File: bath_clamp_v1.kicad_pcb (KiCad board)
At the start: 6 copper layers, 127 x 76.2 mm, 154 parts, among them IC1 DAC53401DSGR, J1 105-1103-001, J2 105-1103-001, J3 105-1103-001, J4 HDMI_A, K1 1462042-8, K2 1462042-8, Q1 MBT3904DW1T1G, Q2 BC856, Q3 MBT3904DW1T1G, Q4 MBT3904DW1T1G, U1 OPA828, U10 LP2951-3.3_SOIC, U11 OPA991S, U12 TCA9555DBR, U13 TCA9555DBR, U14 DG412xUE, U15 OPA828, U16 TMUX6111PWR, U17 DG412xUE, U18 AD8421ARZ, U19 TMUX6136PWR, U2 ADG1208, U20 TMUX6111PWR, U21 TMUX6111PWR, U22 TMUX6136PWR, U23 OPA188xxDBV, U24 LMP8350MA_NOPB, U25 OPA2156xD, U3 G6L-1F-TR-DC5, U4 G6L-1F-TR-DC5, U5 G6L-1F-TR-DC5, U6 24AA025UID, U7 LM337L_SO8, U8 OPA2156xD, U9 MCP1804x-3302xOT

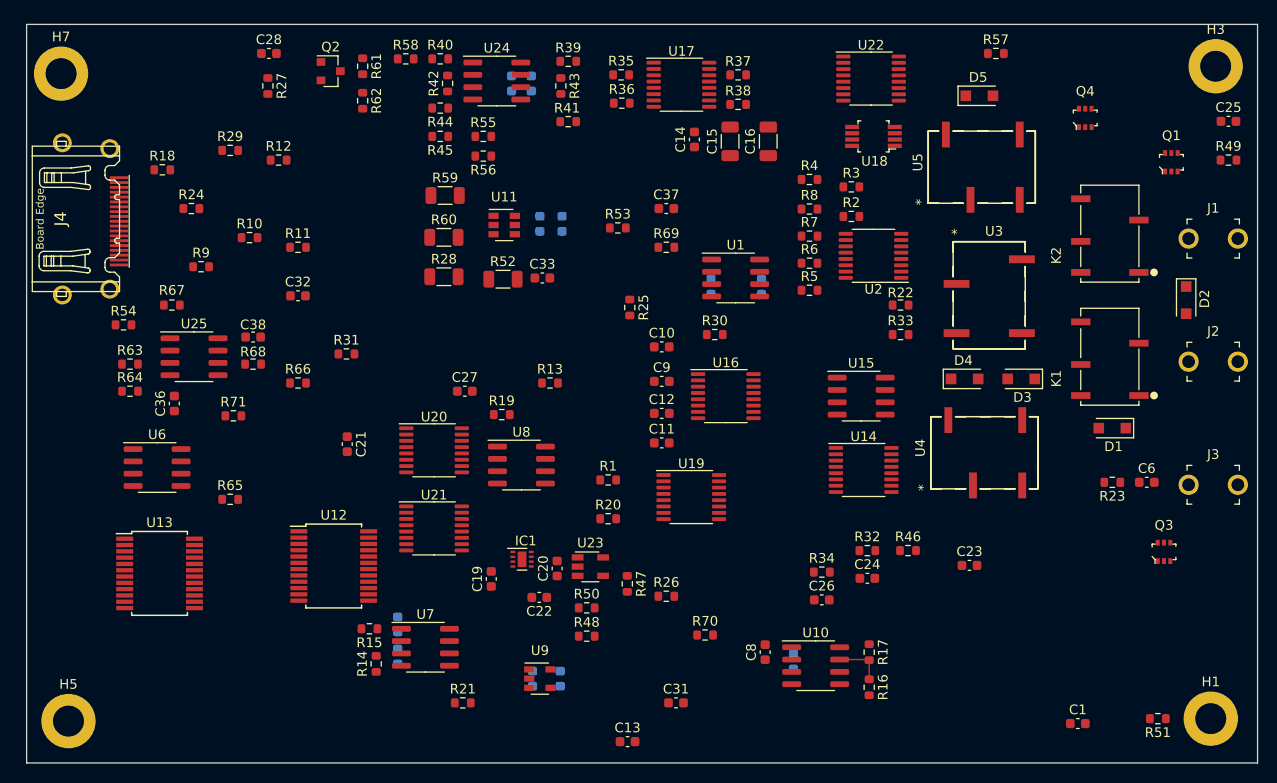
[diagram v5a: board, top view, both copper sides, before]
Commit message: first freerouter trial of routing
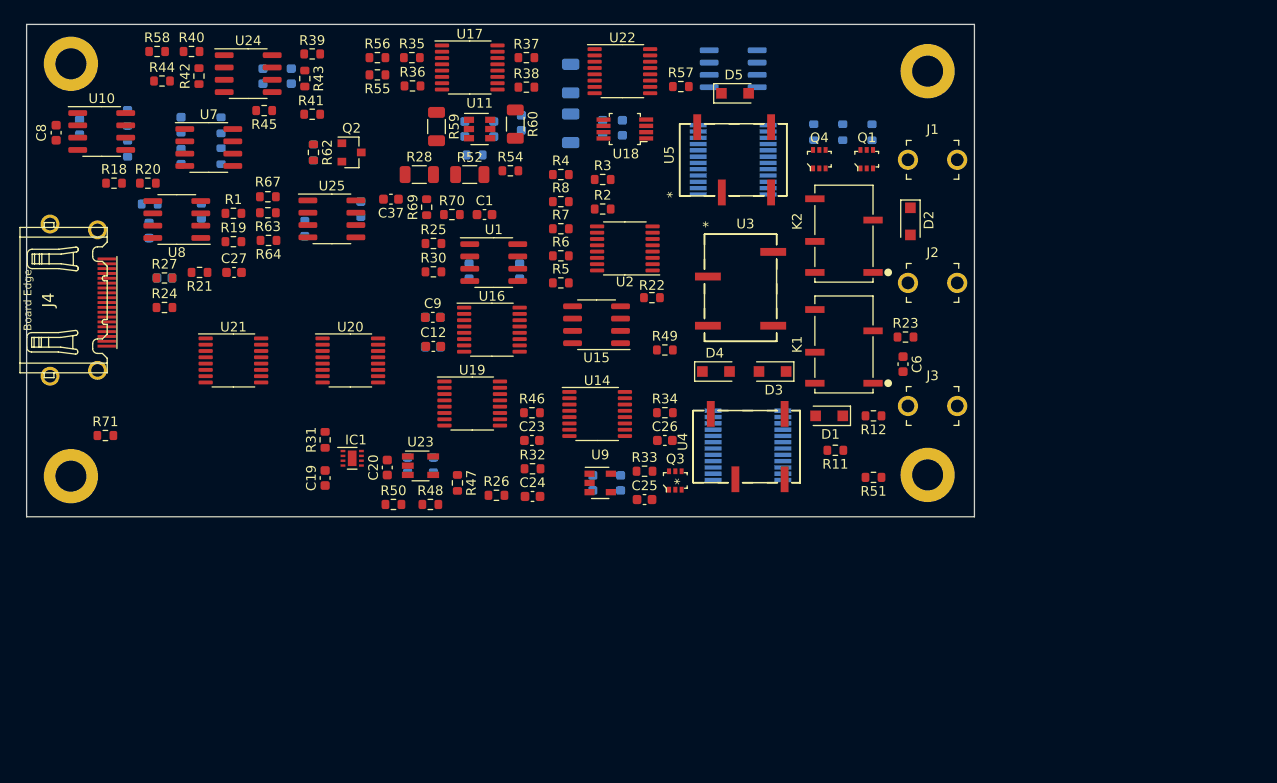
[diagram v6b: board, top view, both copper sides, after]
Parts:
- removed R65, R66, R68: 0, Resistor_SMD:R_0603_1608Metric
- C10, C11, C13, C14, C15, C16, C21, C22, C28, C31, C32, C33, C36, C38, R10, R13, R14, R15, R16, R17, R29, R53, R61, R9, U12, U13, U6: moved to B.Cu
- moved R16 94.6 mm to (10.4, 12.8)
- moved R17 94.3 mm to (10.4, 9.65)
- moved C7 92.0 mm to (5.46, 10.6)
- moved U10 92.0 mm to (7.75, 11.0)
- moved C8 90.7 mm to (3.05, 11.2), turned to 270 degrees
- moved C1 80.7 mm to (47.2, 19.6)
- moved U13 73.0 mm to (72.9, 14.0)
- moved U6 72.3 mm to (72.9, 4.57)
- moved C25 71.8 mm to (63.8, 49.0)
- moved C31 70.5 mm to (18.0, 19.2), turned to 90 degrees
- moved R12 66.8 mm to (87.4, 40.4), turned to 180 degrees
- moved R9 64.7 mm to (81.2, 11.1), turned to 270 degrees
- moved C13 63.3 mm to (61.5, 10.7), turned to 90 degrees
- moved R10 62.2 mm to (84.2, 11.1), turned to 270 degrees
- moved R49 61.4 mm to (65.8, 33.6)
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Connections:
- C1 pad 1: /bath_clamp_v1_1/RF_1 -> Net-(C1-Pad1)
- C1 pad 2: Net-(C1-Pad2) -> /bath_clamp_v1_1/RF_1
- R31 pad 1: GND -> Net-(IC1-Pad1)
- R31 pad 2: Net-(IC1-Pad1) -> GND
- R46 pad 1: Net-(C23-Pad2) -> Net-(C23-Pad1)
- R46 pad 2: Net-(C23-Pad1) -> Net-(C23-Pad2)
- R69 pad 1: Net-(C37-Pad1) -> /bath_clamp_v1_1/compensation_switching/OUT
- R69 pad 2: /bath_clamp_v1_1/compensation_switching/OUT -> Net-(C37-Pad1)
- R70 pad 1: Net-(C1-Pad2) -> /bath_clamp_v1_1/compensation_switching/OUT
- R70 pad 2: /bath_clamp_v1_1/compensation_switching/OUT -> Net-(C1-Pad1)
- U25 pad 5: Net-(R65-Pad1) -> GND
- U25 pad 6: Net-(R66-Pad1) -> GND
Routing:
- net Net-(R16-Pad1): track 5.05 -> 0.00 mm
- net (no net): track 0.00 -> 0.74 mm
- added copper zone on Route14, net +15V
- added copper zone on Route3, net +5V
- added copper zone on Route15, net -15V
- added copper zone on Route2, net GND
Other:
- board size 127 x 76.2 mm -> 97.8 x 50.8 mm
- net class Power added: clearance 0.2032, trace_width 0.508, via_dia 0.889, via_drill 0.381

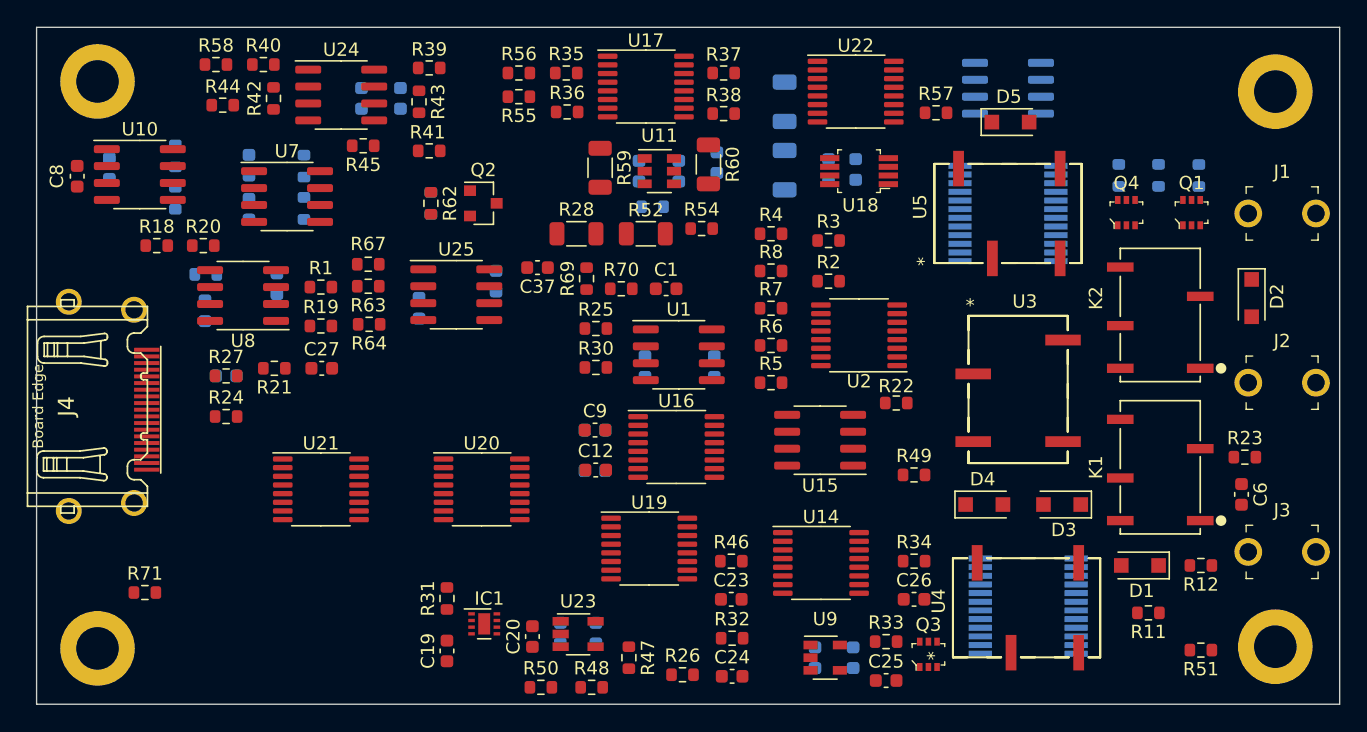
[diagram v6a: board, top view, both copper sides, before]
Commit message: layout updates and 3d models
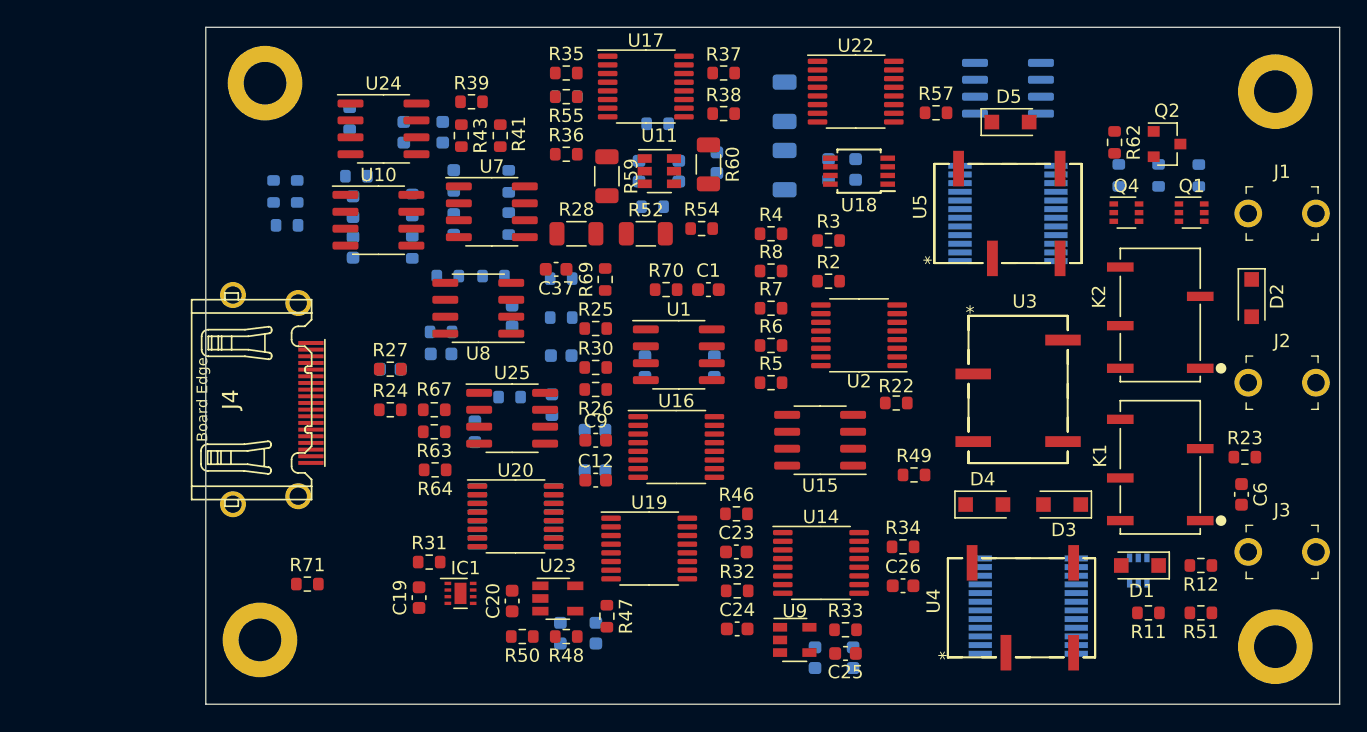
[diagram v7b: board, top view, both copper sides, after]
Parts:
- C27, C8, R1, R18, R19, R20, R21, R40, R42, R44, R45, R56, R58, U21: moved to B.Cu
- Q1, Q4: footprint digikey-footprints:SOT-363 -> Package_TO_SOT_SMD:SOT-363_SC-70-6
- Q3: footprint digikey-footprints:SOT-363 -> Package_TO_SOT_SMD:SOT-363_SC-70-6; moved to B.Cu
- U18: footprint digikey-footprints:TSSOP-8_W3mm -> Package_SO:TSSOP-8_3x3mm_P0.65mm
- moved R62 51.5 mm to (80.9, 8.64)
- moved Q2 51.5 mm to (84.8, 8.76)
- moved R26 22.4 mm to (42.0, 27.2), turned to 180 degrees
- moved R18 22.0 mm to (30.9, 18.7)
- moved R20 21.9 mm to (34.3, 18.7)
- moved C8 21.4 mm to (23.7, 16.5), turned to 90 degrees
- moved C7 18.5 mm to (23.7, 13.5)
- moved U10 18.2 mm to (25.7, 14.5)
- moved R29 18.2 mm to (30.4, 22.9)
- moved R16 18.2 mm to (28.2, 16.5)
- moved R17 18.2 mm to (28.2, 13.3)
- moved R1 18.0 mm to (39.4, 18.9)
- moved R19 18.0 mm to (39.4, 21.8)
- moved R61 18.0 mm to (46.6, 7.24), turned to 0 degrees
- moved C32 18.0 mm to (30.4, 24.5), turned to 0 degrees
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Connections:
- net /bath_clamp_v1_1/compensation_switching/IN renamed /bath_clamp_v1_1/F_MUX_OUT
- net /bath_clamp_v1_1/compensation_switching/OUT renamed /bath_clamp_v1_1/V_GND
- net /bath_clamp_v1_1/feedback_buffer/IN renamed /bath_clamp_v1_1/P1
- net Net-(J1-Pad1) renamed /bath_clamp_v1_1/P2_OUT
- net Net-(J2-Pad1) renamed /bath_clamp_v1_1/P1_OUT
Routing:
- net (no net): track 0.74 -> 0.00 mm
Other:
- board size 97.8 x 50.8 mm -> 85.1 x 50.8 mm

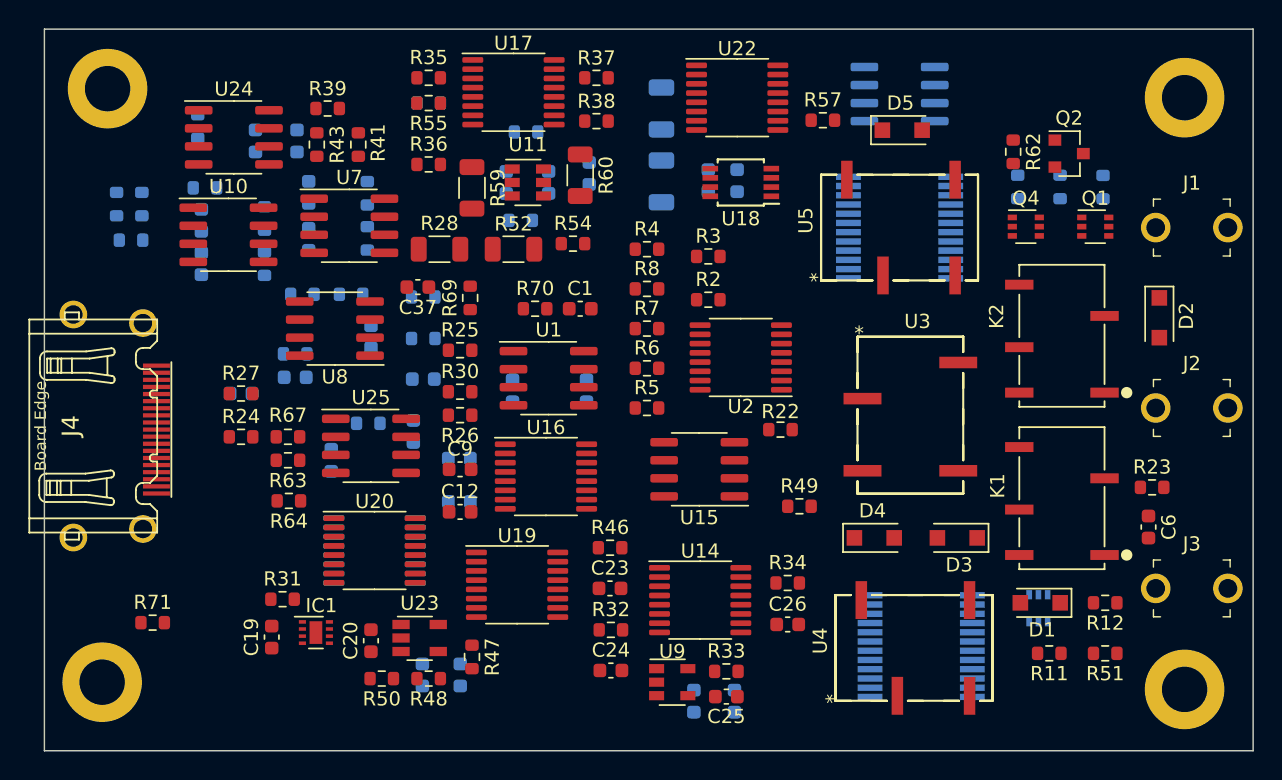
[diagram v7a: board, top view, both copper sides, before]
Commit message: updates to README
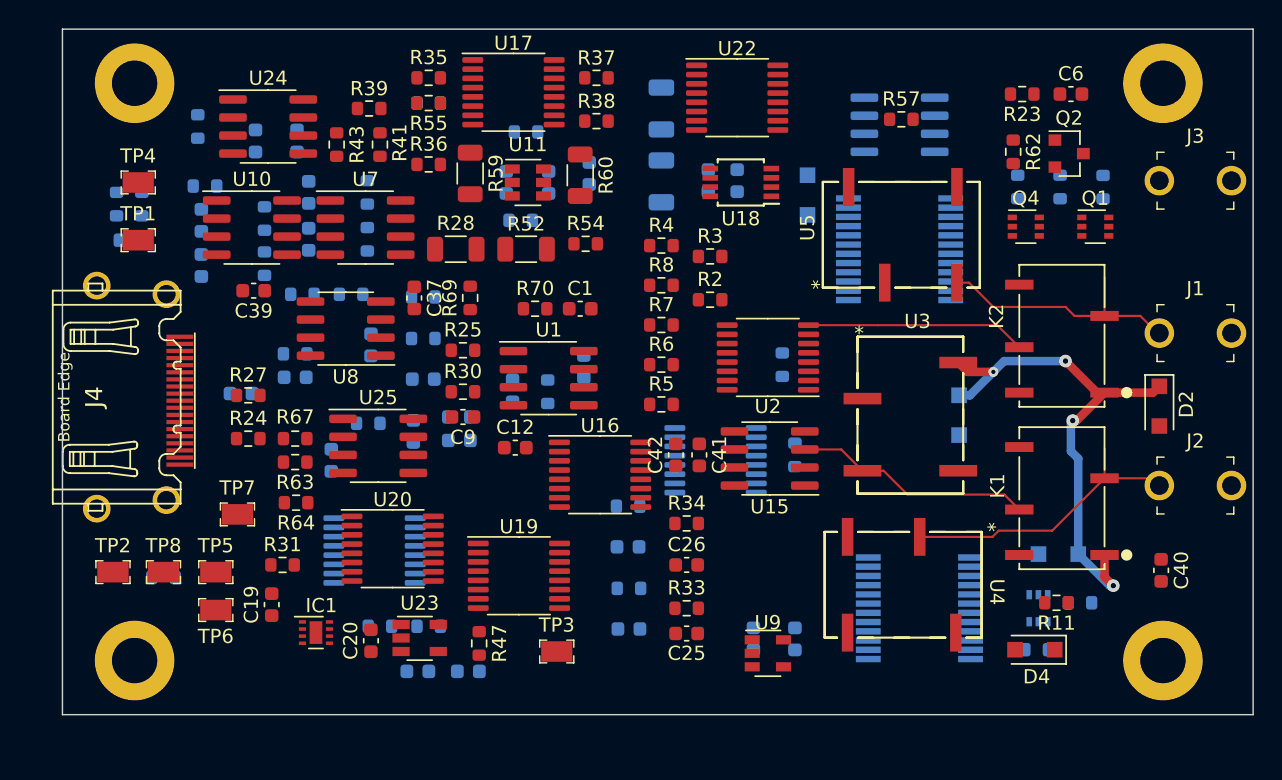
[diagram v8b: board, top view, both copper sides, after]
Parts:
- added C39: 0.1u, Capacitor_SMD:C_0603_1608Metric, F.Cu at (27.4, 18.4)
- added C40: 0.1u, Capacitor_SMD:C_0603_1608Metric, F.Cu at (91.3, 38.1)
- added C41: 0.1u, Capacitor_SMD:C_0603_1608Metric, F.Cu at (58.8, 30.0)
- added C42: 0.1u, Capacitor_SMD:C_0603_1608Metric, F.Cu at (57.1, 30.0)
- added TP1: RCT-0C, digikey-footprints:PROBE_PAD_0805, F.Cu at (19.3, 14.9)
- added TP2: RCT-0C, digikey-footprints:PROBE_PAD_0805, F.Cu at (17.5, 38.2)
- added TP3: RCT-0C, digikey-footprints:PROBE_PAD_0805, F.Cu at (48.8, 43.8)
- added TP4: RCT-0C, digikey-footprints:PROBE_PAD_0805, F.Cu at (19.3, 10.8)
- added TP5: RCT-0C, digikey-footprints:PROBE_PAD_0805, F.Cu at (24.8, 38.2)
- added TP6: RCT-0C, digikey-footprints:PROBE_PAD_0805, F.Cu at (24.8, 40.9)
- added TP7: RCT-0C, digikey-footprints:PROBE_PAD_0805, F.Cu at (26.3, 34.2)
- added TP8: RCT-0C, digikey-footprints:PROBE_PAD_0805, F.Cu at (21.1, 38.2)
- C23: value 70p -> 68p; moved to B.Cu
- C24, D1, D3, D5, R12, R22, R26, R32, R46, R48, R49, R50, R51, R71, U14: moved to B.Cu
- R39, R40: value 1820 -> 1500
- moved C6 31.0 mm to (85.0, 4.57), turned to 0 degrees
- moved R23 29.2 mm to (81.5, 4.57), turned to 180 degrees
- moved J3 28.7 mm to (93.7, 10.7)
- moved D4 13.8 mm to (82.4, 43.7), turned to 180 degrees
- moved U14 9.90 mm to (59.9, 30.4)
- moved D3 8.64 mm to (77.1, 27.2), turned to 270 degrees
- moved C26 8.25 mm to (57.9, 37.7)
- moved R34 8.25 mm to (57.9, 34.8)
- moved D5 8.08 mm to (66.4, 11.7), turned to 270 degrees
- moved J1 7.43 mm to (93.7, 21.4)
- moved U9 7.03 mm to (63.6, 43.9)
- moved R26 6.39 mm to (48.1, 25.5), turned to 90 degrees
- moved D2 6.22 mm to (91.2, 26.5)
- moved C5 6.11 mm to (65.5, 42.9)
- moved C4 6.06 mm to (62.6, 42.9)
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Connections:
- U12 pad 17: /bath_clamp_v1_1/G1 -> /bath_clamp_v1_1/RF1
- U12 pad 18: /bath_clamp_v1_1/G2 -> /bath_clamp_v1_1/RF2
- U12 pad 19: /bath_clamp_v1_1/G3 -> /bath_clamp_v1_1/RF3
- U12 pad 20: /bath_clamp_v1_1/FDBK -> /bath_clamp_v1_1/RF4
- U13 pad 13: /bath_clamp_v1_1/RF1 -> /bath_clamp_v1_1/G1
- U13 pad 14: /bath_clamp_v1_1/RF2 -> /bath_clamp_v1_1/G2
- U13 pad 15: /bath_clamp_v1_1/RF3 -> /bath_clamp_v1_1/G3
- U13 pad 16: /bath_clamp_v1_1/RF4 -> /bath_clamp_v1_1/FDBK
- U14 pad 12: (no net) -> +3V3
- U14 pad 13: (no net) -> +15V
- U14 pad 4: (no net) -> -15V
- U14 pad 5: (no net) -> GND
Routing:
- net +5V: track 0.00 -> 37.6 mm, vias 0 -> 4
- net /bath_clamp_v1_1/P1_OUT: track 0.00 -> 20.9 mm
- net /bath_clamp_v1_1/P2_OUT: track 0.00 -> 18.3 mm
- net /bath_clamp_v1_1/P1: track 0.00 -> 16.9 mm
- net /bath_clamp_v1_1/P2: track 0.00 -> 15.5 mm
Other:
- board size 85.1 x 50.8 mm -> 83.8 x 48.3 mm
- net class Default: clearance 0.15 -> 0.1524; trace_width 0.15 -> 0.1524
- net class Power: clearance 0.2032 -> 0.1778; trace_width 0.508 -> 0.3048
- net class cap_sensitive added: clearance 0.3048, trace_width 0.1524, via_dia 0.7, via_drill 0.3
- rule trace_clearance: 0.15 -> 0.1524
